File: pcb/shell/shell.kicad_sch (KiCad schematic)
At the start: 220 parts, among them J1 Conn_01x11, J2 Conn_01x11

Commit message: hid reference designators, simplified footprint silkscreens, added license, added rocks and stones
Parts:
- D1, D10, D11, D12, D13, D14, D15, D16, D17, D18, D19, D2, D20, D21, D22, D23, D24, D25, D26, D27, D28, D29, D3, D30, D31, D32, D33, D34, D35, D36, D37, D38, D39, D4, D40, D41, D42, D43, D44, D45, D46, D47, D48, D49, D5, D50, D51, D52, D53, D54, D55, D56, D57, D58, D59, D6, D60, D61, D7, D8, D9: footprint Diode_SMD:D_SOD-123 -> barnacle:D_SOD-123-minimal
- MX1, MX10, MX11, MX12, MX14, MX15, MX16, MX17, MX18, MX19, MX2, MX20, MX21, MX22, MX23, MX26, MX27, MX28, MX29, MX3, MX30, MX31, MX32, MX33, MX34, MX35, MX38, MX39, MX4, MX40, MX41, MX42, MX43, MX44, MX45, MX46, MX47, MX49, MX5, MX52, MX54, MX55, MX56, MX57, MX6, MX7, MX8, MX9: footprint PCM_marbastlib-mx:SW_MX_HS_CPG151101S11_1u -> PCM_marbastlib-mx:SW_MX_HS_S_CPG151101S11_1u
- MX13, MX24, MX61: footprint PCM_marbastlib-mx:SW_MX_HS_CPG151101S11_1.5u -> PCM_marbastlib-mx:SW_MX_HS_S_CPG151101S11_1u
- MX25, MX36, MX37: footprint PCM_marbastlib-mx:SW_MX_HS_CPG151101S11_1.75u -> PCM_marbastlib-mx:SW_MX_HS_S_CPG151101S11_1u
- MX48, MX50, MX51, MX53, MX58, MX59, MX60: footprint PCM_marbastlib-mx:SW_MX_HS_CPG151101S11_1.25u -> PCM_marbastlib-mx:SW_MX_HS_S_CPG151101S11_1u
- UG1, UG10, UG11, UG12, UG13, UG14, UG15, UG16, UG17, UG18, UG19, UG2, UG20, UG21, UG22, UG23, UG24, UG25, UG26, UG27, UG28, UG3, UG4, UG5, UG6, UG7, UG8, UG9: footprint LED_SMD:LED_SK6812_PLCC4_5.0x5.0mm_P3.2mm -> barnacle:LED_SK6812_PLCC4_5.0x5.0mm_P3.2mm-minimal

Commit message: changed sk6812 footprints to be also compatible with sk6812 mini (v1.2)
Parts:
- UG1, UG10, UG11, UG12, UG13, UG14, UG15, UG16, UG17, UG18, UG19, UG2, UG20, UG21, UG22, UG23, UG24, UG25, UG26, UG27, UG28, UG3, UG4, UG5, UG6, UG7, UG8, UG9: footprint barnacle:LED_SK6812_PLCC4_5.0x5.0mm_P3.2mm-minimal -> barnacle:LED_SK6812-combi
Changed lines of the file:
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@@
 			)
 		)
-		(property "Footprint" "barnacle:LED_SK6812_PLCC4_5.0x5.0mm_P3.2mm-minimal"
+		(property "Footprint" "barnacle:LED_SK6812-combi"
 			(at 180.34 195.58 0)
 			(effects
@@
 			)
 		)
-		(property "Footprint" "barnacle:LED_SK6812_PLCC4_5.0x5.0mm_P3.2mm-minimal"
+		(property "Footprint" "barnacle:LED_SK6812-combi"
 			(at 88.9 195.58 0)
 			(effects
@@
 			)
 		)
-		(property "Footprint" "barnacle:LED_SK6812_PLCC4_5.0x5.0mm_P3.2mm-minimal"
+		(property "Footprint" "barnacle:LED_SK6812-combi"
 			(at 134.62 195.58 0)
 			(effects
@@
 			)
 		)
-		(property "Footprint" "barnacle:LED_SK6812_PLCC4_5.0x5.0mm_P3.2mm-minimal"
+		(property "Footprint" "barnacle:LED_SK6812-combi"
 			(at 149.86 195.58 0)
 			(effects
@@
 			)
 		)
-		(property "Footprint" "barnacle:LED_SK6812_PLCC4_5.0x5.0mm_P3.2mm-minimal"
+		(property "Footprint" "barnacle:LED_SK6812-combi"
 			(at 153.67 218.44 0)
 			(effects
@@
 			)
 		)
-		(property "Footprint" "barnacle:LED_SK6812_PLCC4_5.0x5.0mm_P3.2mm-minimal"
+		(property "Footprint" "barnacle:LED_SK6812-combi"
 			(at 226.06 195.58 0)
 			(effects
@@
 			)
 		)
-		(property "Footprint" "barnacle:LED_SK6812_PLCC4_5.0x5.0mm_P3.2mm-minimal"
+		(property "Footprint" "barnacle:LED_SK6812-combi"
 			(at 210.82 195.58 0)
 			(effects
@@
 			)
 		)
-		(property "Footprint" "barnacle:LED_SK6812_PLCC4_5.0x5.0mm_P3.2mm-minimal"
+		(property "Footprint" "barnacle:LED_SK6812-combi"
 			(at 58.42 195.58 0)
 			(effects
@@
 			)
 		)
-		(property "Footprint" "barnacle:LED_SK6812_PLCC4_5.0x5.0mm_P3.2mm-minimal"
+		(property "Footprint" "barnacle:LED_SK6812-combi"
 			(at 88.9 218.44 0)
 			(effects
@@
 			)
 		)
-		(property "Footprint" "barnacle:LED_SK6812_PLCC4_5.0x5.0mm_P3.2mm-minimal"
+		(property "Footprint" "barnacle:LED_SK6812-combi"
 			(at 58.42 218.44 0)
 			(effects
@@
 			)
 		)
-		(property "Footprint" "barnacle:LED_SK6812_PLCC4_5.0x5.0mm_P3.2mm-minimal"
+		(property "Footprint" "barnacle:LED_SK6812-combi"
 			(at 153.67 172.72 0)
 			(effects
@@
 			)
 		)
-		(property "Footprint" "barnacle:LED_SK6812_PLCC4_5.0x5.0mm_P3.2mm-minimal"
+		(property "Footprint" "barnacle:LED_SK6812-combi"
 			(at 73.66 195.58 0)
 			(effects
@@
 			)
 		)
-		(property "Footprint" "barnacle:LED_SK6812_PLCC4_5.0x5.0mm_P3.2mm-minimal"
+		(property "Footprint" "barnacle:LED_SK6812-combi"
 			(at 123.19 218.44 0)
 			(effects
@@
 			)
 		)
-		(property "Footprint" "barnacle:LED_SK6812_PLCC4_5.0x5.0mm_P3.2mm-minimal"
+		(property "Footprint" "barnacle:LED_SK6812-combi"
 			(at 168.91 172.72 0)
 			(effects
@@
 			)
 		)
-		(property "Footprint" "barnacle:LED_SK6812_PLCC4_5.0x5.0mm_P3.2mm-minimal"
+		(property "Footprint" "barnacle:LED_SK6812-combi"
 			(at 88.9 172.72 0)
 			(effects
@@
 			)
 		)
-		(property "Footprint" "barnacle:LED_SK6812_PLCC4_5.0x5.0mm_P3.2mm-minimal"
+		(property "Footprint" "barnacle:LED_SK6812-combi"
 			(at 195.58 195.58 0)
 			(effects
@@
 			)
 		)
-		(property "Footprint" "barnacle:LED_SK6812_PLCC4_5.0x5.0mm_P3.2mm-minimal"
+		(property "Footprint" "barnacle:LED_SK6812-combi"
 			(at 104.14 195.58 0)
 			(effects
@@
 			)
 		)
-		(property "Footprint" "barnacle:LED_SK6812_PLCC4_5.0x5.0mm_P3.2mm-minimal"
+		(property "Footprint" "barnacle:LED_SK6812-combi"
 			(at 104.14 172.72 0)
 			(effects
@@
 			)
 		)
-		(property "Footprint" "barnacle:LED_SK6812_PLCC4_5.0x5.0mm_P3.2mm-minimal"
+		(property "Footprint" "barnacle:LED_SK6812-combi"
 			(at 119.38 195.58 0)
 			(effects
@@
 			)
 		)
-		(property "Footprint" "barnacle:LED_SK6812_PLCC4_5.0x5.0mm_P3.2mm-minimal"
+		(property "Footprint" "barnacle:LED_SK6812-combi"
 			(at 168.91 218.44 0)
 			(effects
@@
 			)
 		)
-		(property "Footprint" "barnacle:LED_SK6812_PLCC4_5.0x5.0mm_P3.2mm-minimal"
+		(property "Footprint" "barnacle:LED_SK6812-combi"
 			(at 73.66 172.72 0)
 			(effects
@@
 			)
 		)
-		(property "Footprint" "barnacle:LED_SK6812_PLCC4_5.0x5.0mm_P3.2mm-minimal"
+		(property "Footprint" "barnacle:LED_SK6812-combi"
 			(at 73.66 218.44 0)
 			(effects
@@
 			)
 		)
-		(property "Footprint" "barnacle:LED_SK6812_PLCC4_5.0x5.0mm_P3.2mm-minimal"
+		(property "Footprint" "barnacle:LED_SK6812-combi"
 			(at 58.42 172.72 0)
 			(effects
@@
 			)
 		)
-		(property "Footprint" "barnacle:LED_SK6812_PLCC4_5.0x5.0mm_P3.2mm-minimal"
+		(property "Footprint" "barnacle:LED_SK6812-combi"
 			(at 138.43 172.72 0)
 			(effects
@@
 			)
 		)
-		(property "Footprint" "barnacle:LED_SK6812_PLCC4_5.0x5.0mm_P3.2mm-minimal"
+		(property "Footprint" "barnacle:LED_SK6812-combi"
 			(at 119.38 172.72 0)
 			(effects
@@
 			)
 		)
-		(property "Footprint" "barnacle:LED_SK6812_PLCC4_5.0x5.0mm_P3.2mm-minimal"
+		(property "Footprint" "barnacle:LED_SK6812-combi"
 			(at 165.1 195.58 0)
 			(effects
@@
 			)
 		)
-		(property "Footprint" "barnacle:LED_SK6812_PLCC4_5.0x5.0mm_P3.2mm-minimal"
+		(property "Footprint" "barnacle:LED_SK6812-combi"
 			(at 107.95 218.44 0)
 			(effects
@@
 			)
 		)
-		(property "Footprint" "barnacle:LED_SK6812_PLCC4_5.0x5.0mm_P3.2mm-minimal"
+		(property "Footprint" "barnacle:LED_SK6812-combi"
 			(at 138.43 218.44 0)
 			(effects

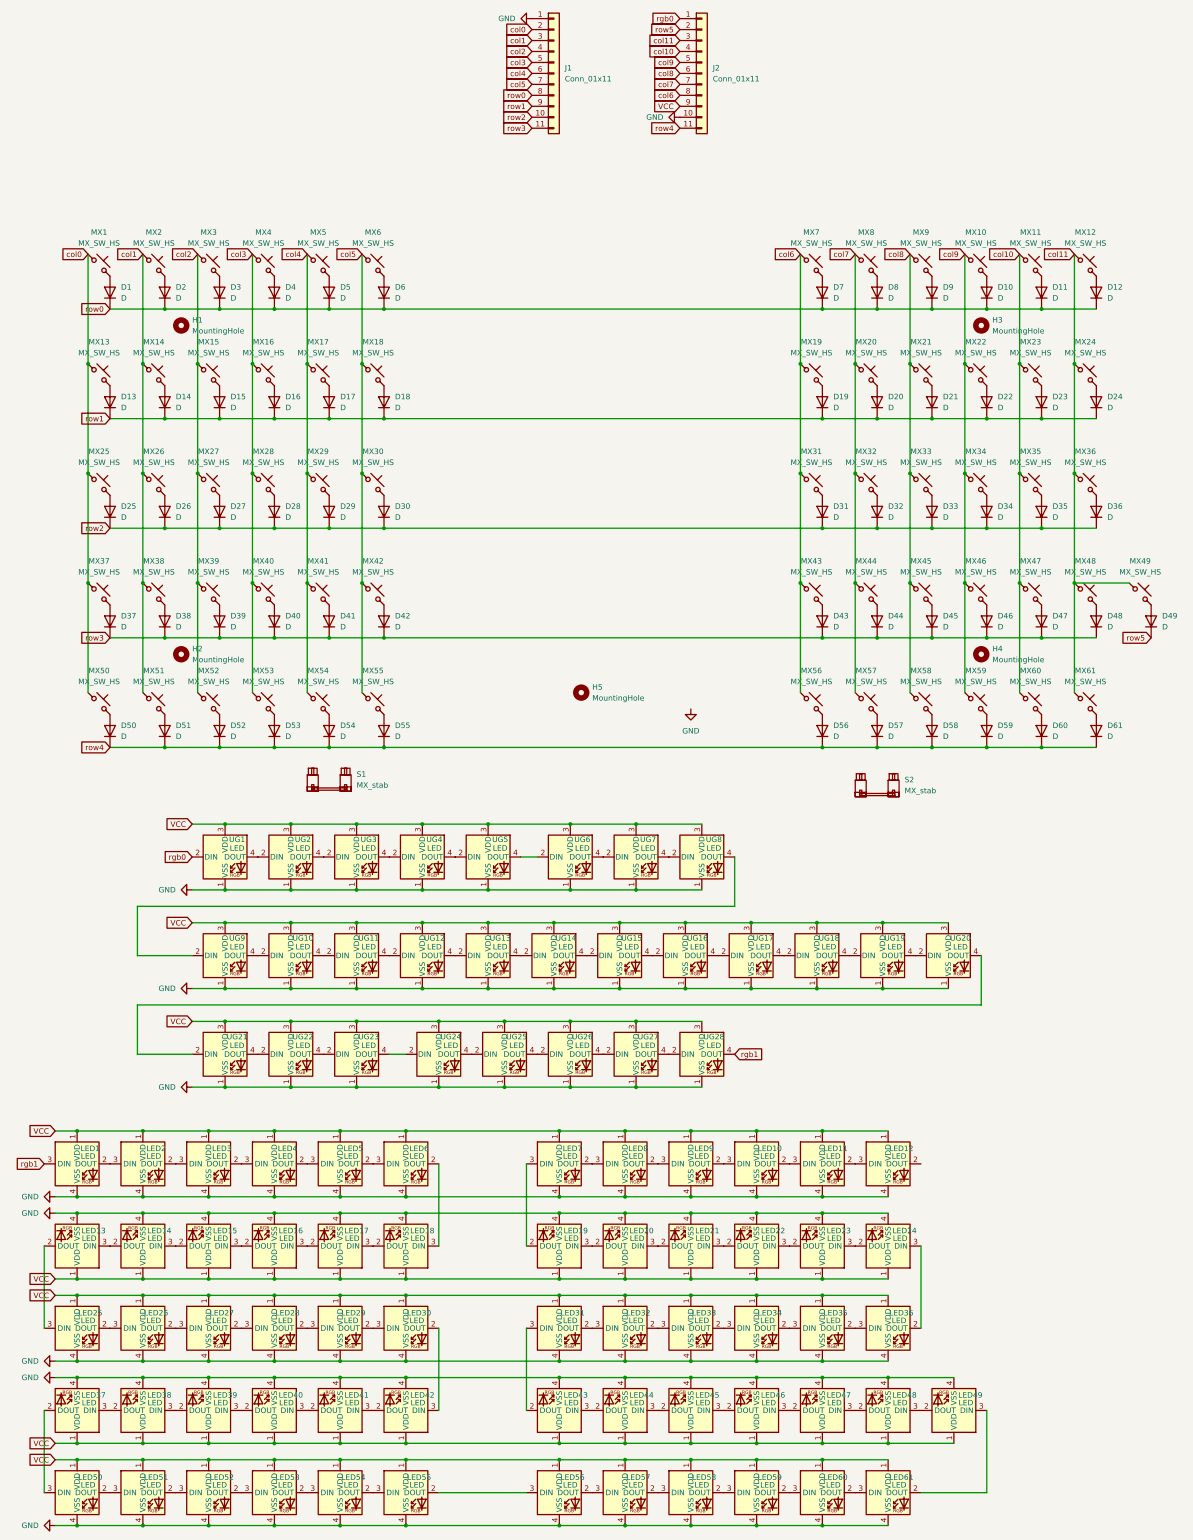
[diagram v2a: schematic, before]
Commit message: updated pcb to only use sk6812 mini-e
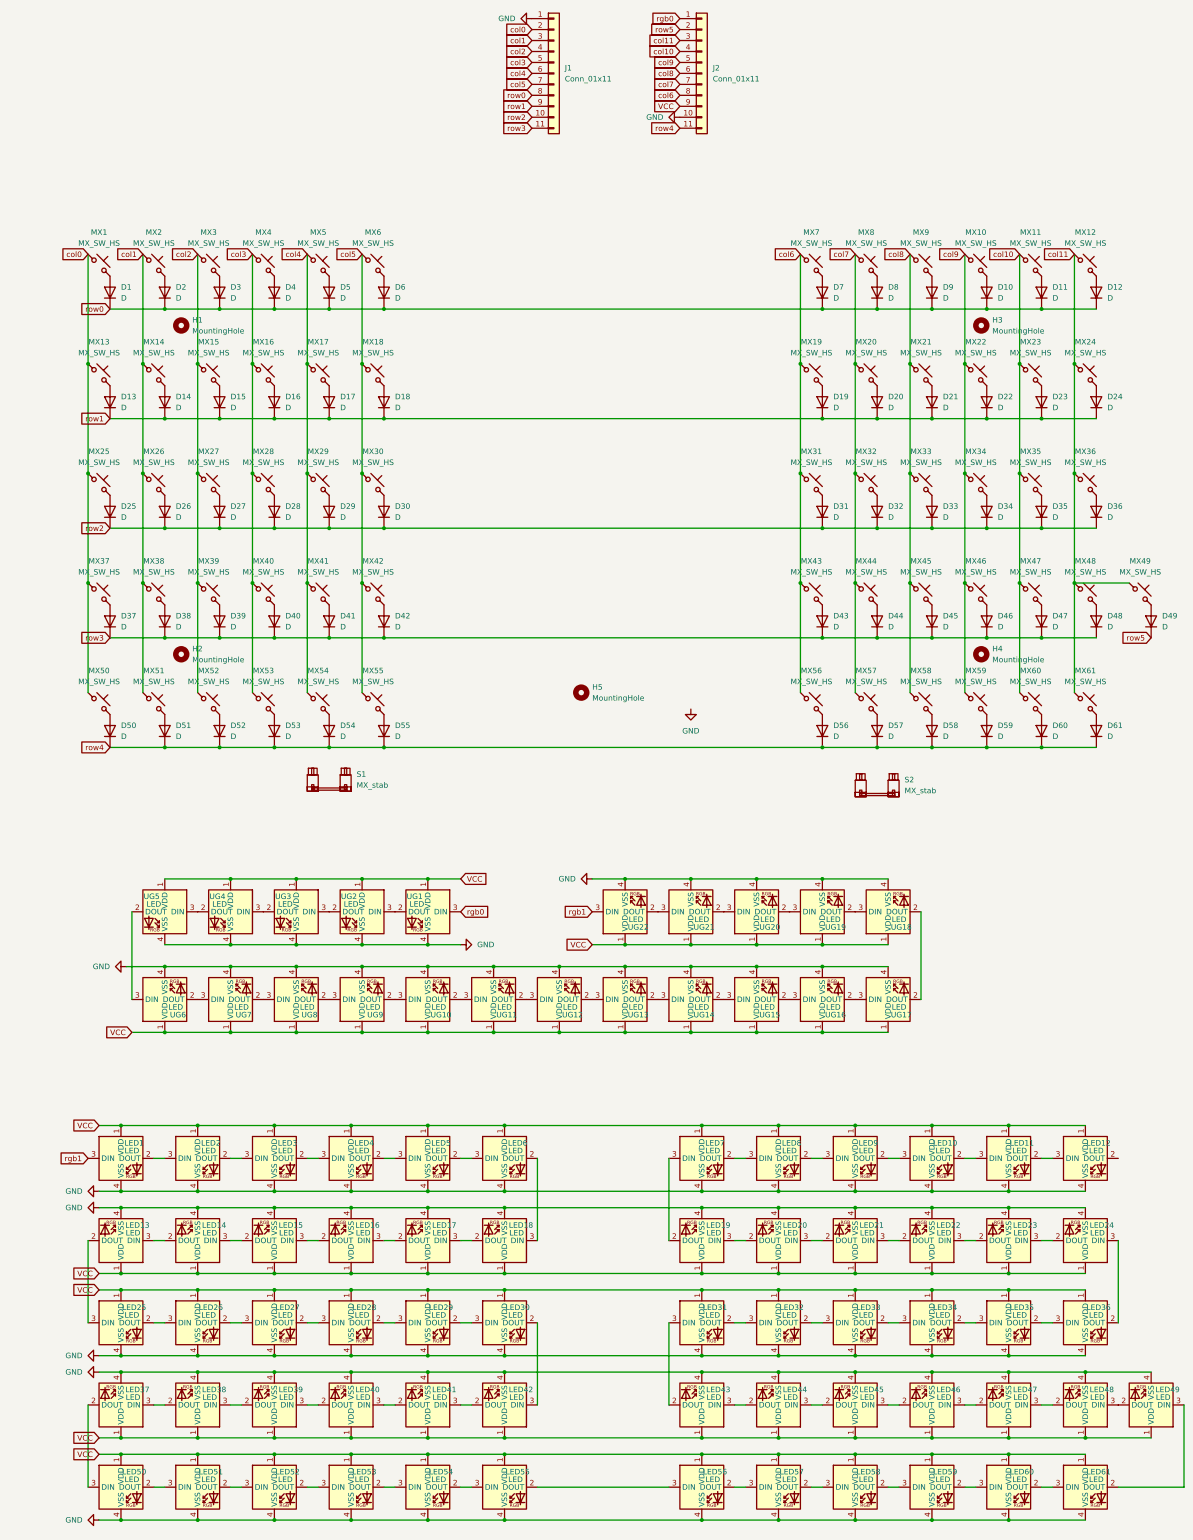
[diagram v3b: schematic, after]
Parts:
- removed UG1, UG10, UG11, UG12, UG13, UG14, UG15, UG16, UG17, UG18, UG19, UG2, UG20, UG21, UG22, UG23, UG24, UG25, UG26, UG27, UG28, UG3, UG4, UG5, UG6, UG7, UG8, UG9: LED, barnacle:LED_SK6812-combi, symbol LED:SK6812
- added UG1, UG10, UG11, UG12, UG13, UG14, UG15, UG16, UG17, UG18, UG19, UG2, UG20, UG21, UG22, UG3, UG4, UG5, UG6, UG7, UG8, UG9: LED, barnacle:sk6812 mini-e towards-facing, symbol PCM_marbastlib-mx:MX_SK6812MINI-E
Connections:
- net GND: now also UG1.4 (VSS), UG10.4 (VSS), UG11.4 (VSS), UG12.4 (VSS), UG13.4 (VSS), UG14.4 (VSS), UG15.4 (VSS), UG16.4 (VSS), UG17.4 (VSS), UG18.4 (VSS), UG19.4 (VSS), UG2.4 (VSS), UG20.4 (VSS), UG21.4 (VSS), UG22.4 (VSS), UG3.4 (VSS), UG4.4 (VSS), UG5.4 (VSS), UG6.4 (VSS), UG7.4 (VSS), UG8.4 (VSS), UG9.4 (VSS)
- net VCC: now also UG1.1 (VDD), UG10.1 (VDD), UG11.1 (VDD), UG12.1 (VDD), UG13.1 (VDD), UG14.1 (VDD), UG15.1 (VDD), UG16.1 (VDD), UG17.1 (VDD), UG18.1 (VDD), UG19.1 (VDD), UG2.1 (VDD), UG20.1 (VDD), UG21.1 (VDD), UG22.1 (VDD), UG3.1 (VDD), UG4.1 (VDD), UG5.1 (VDD), UG6.1 (VDD), UG7.1 (VDD), UG8.1 (VDD), UG9.1 (VDD)
- net rgb0: now also UG1.3 (DIN)
- net rgb1: now also UG22.3 (DIN)
- new net: UG14.2 (DOUT), UG15.3 (DIN)
- new net: UG13.2 (DOUT), UG14.3 (DIN)
- new net: UG20.3 (DIN), UG21.2 (DOUT)
- new net: UG21.3 (DIN), UG22.2 (DOUT)
- new net: UG7.2 (DOUT), UG8.3 (DIN)
- new net: UG6.2 (DOUT), UG7.3 (DIN)
- new net: UG17.2 (DOUT), UG18.2 (DOUT)
- new net: UG16.2 (DOUT), UG17.3 (DIN)
- new net: UG4.2 (DOUT), UG5.3 (DIN)
- new net: UG3.2 (DOUT), UG4.3 (DIN)
- new net: UG2.2 (DOUT), UG3.3 (DIN)
- new net: UG1.2 (DOUT), UG2.3 (DIN)
- new net: UG19.3 (DIN), UG20.2 (DOUT)
- new net: UG12.2 (DOUT), UG13.3 (DIN)
- new net: UG11.2 (DOUT), UG12.3 (DIN)
- new net: UG5.2 (DOUT), UG6.3 (DIN)
- new net: UG10.2 (DOUT), UG11.3 (DIN)
- new net: UG15.2 (DOUT), UG16.3 (DIN)
- new net: UG8.2 (DOUT), UG9.3 (DIN)
- new net: UG18.3 (DIN), UG19.2 (DOUT)
- new net: UG10.3 (DIN), UG9.2 (DOUT)
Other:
- moved on the sheet: LED1, LED10, LED11, LED12, LED13, LED14, LED15, LED16, LED17, LED18, LED19, LED2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

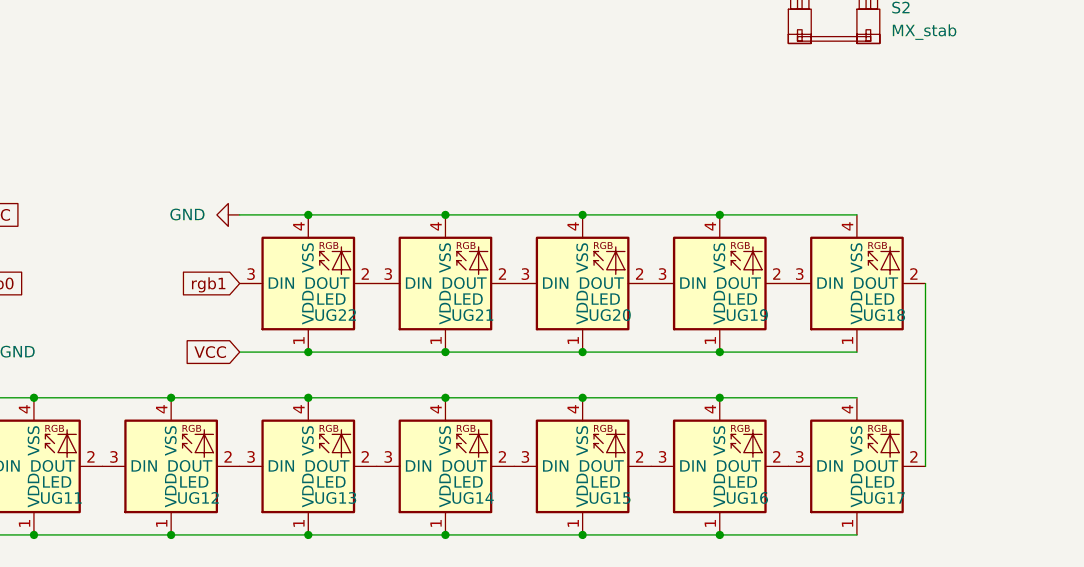
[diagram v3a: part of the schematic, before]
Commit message: fixed rotation of top row underglow leds
sigh…
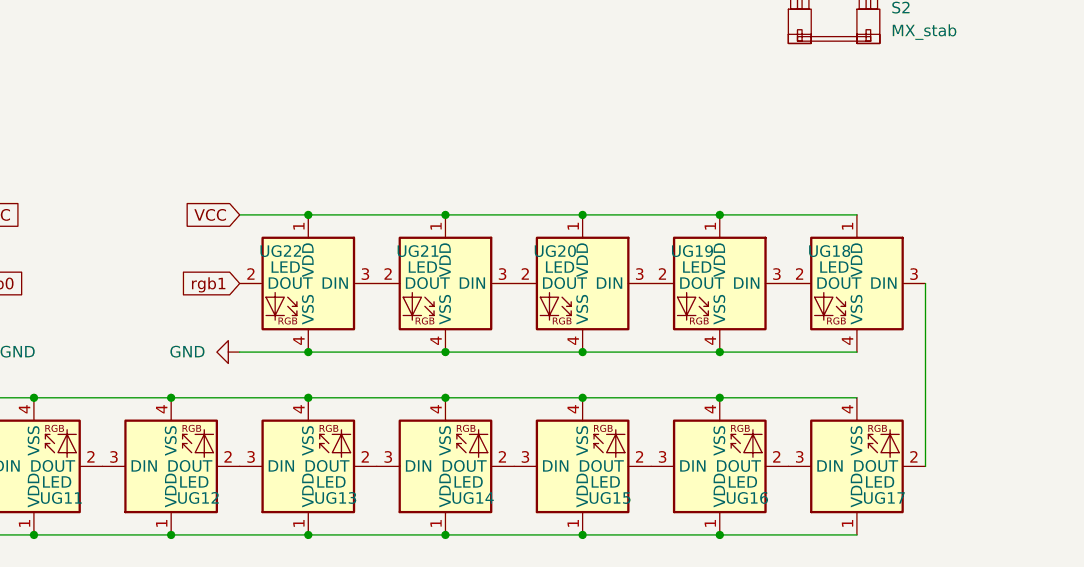
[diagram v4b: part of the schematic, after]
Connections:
- net rgb1: now also UG22.2 (DOUT); no longer UG22.3 (DIN)
- net at UG21.2 (DOUT): now also UG22.3 (DIN); no longer UG20.3 (DIN)
- net at UG21.3 (DIN): now also UG20.2 (DOUT); no longer UG22.2 (DOUT)
- net at UG17.2 (DOUT): now also UG18.3 (DIN); no longer UG18.2 (DOUT)
- net at UG19.3 (DIN): now also UG18.2 (DOUT); no longer UG20.2 (DOUT)
- net at UG19.2 (DOUT): now also UG20.3 (DIN); no longer UG18.3 (DIN)
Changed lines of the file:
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@@
 	(global_label "VCC"
 		(shape input)
-		(at 142.24 185.42 180)
+		(at 142.24 170.18 180)
 		(fields_autoplaced yes)
 		(effects
@@
 		)
 		(property "Intersheetrefs" "${INTERSHEET_REFS}"
-			(at 135.6262 185.42 0)
+			(at 135.6262 170.18 0)
 			(effects
 				(font
@@
 		(lib_id "PCM_marbastlib-mx:MX_SK6812MINI-E")
 		(at 165.1 177.8 0)
-		(mirror x)
+		(mirror y)
 		(unit 1)
 		(exclude_from_sim no)
@@
 		(dnp no)
 		(property "Reference" "UG21"
-			(at 168.148 181.356 0)
+			(at 162.052 174.244 0)
 			(effects
 				(font
@@
 		)
 		(property "Value" "LED"
-			(at 167.64 179.578 0)
+			(at 162.56 176.022 0)
 			(effects
 				(font
@@
 		(lib_id "PCM_marbastlib-mx:MX_SK6812MINI-E")
 		(at 180.34 177.8 0)
-		(mirror x)
+		(mirror y)
 		(unit 1)
 		(exclude_from_sim no)
@@
 		(dnp no)
 		(property "Reference" "UG20"
-			(at 183.388 181.356 0)
+			(at 177.292 174.244 0)
 			(effects
 				(font
@@
 		)
 		(property "Value" "LED"
-			(at 182.88 179.578 0)
+			(at 177.8 176.022 0)
 			(effects
 				(font
@@
 	(symbol
 		(lib_id "power:GND")
-		(at 142.24 170.18 270)
+		(at 142.24 185.42 270)
 		(unit 1)
 		(exclude_from_sim no)
@@
 		(fields_autoplaced yes)
 		(property "Reference" "#PWR010"
-			(at 135.89 170.18 0)
+			(at 135.89 185.42 0)
 			(effects
 				(font
@@
 		)
 		(property "Value" "GND"
-			(at 138.43 170.1799 90)
+			(at 138.43 185.4199 90)
 			(effects
 				(font
@@
 		)
 		(property "Footprint" ""
-			(at 142.24 170.18 0)
+			(at 142.24 185.42 0)
 			(effects
 				(font
@@
 		)
 		(property "Datasheet" ""
-			(at 142.24 170.18 0)
+			(at 142.24 185.42 0)
 			(effects
 				(font
@@
 		)
 		(property "Description" "Power symbol creates a global label with name \"GND\" , ground"
-			(at 142.24 170.18 0)
+			(at 142.24 185.42 0)
 			(effects
 				(font
@@
 		(lib_id "PCM_marbastlib-mx:MX_SK6812MINI-E")
 		(at 195.58 177.8 0)
-		(mirror x)
+		(mirror y)
 		(unit 1)
 		(exclude_from_sim no)
@@
 		(dnp no)
 		(property "Reference" "UG19"
-			(at 198.628 181.356 0)
+			(at 192.532 174.244 0)
 			(effects
 				(font
@@
 		)
 		(property "Value" "LED"
-			(at 198.12 179.578 0)
+			(at 193.04 176.022 0)
 			(effects
 				(font
@@
 		(lib_id "PCM_marbastlib-mx:MX_SK6812MINI-E")
 		(at 149.86 177.8 0)
-		(mirror x)
+		(mirror y)
 		(unit 1)
 		(exclude_from_sim no)
@@
 		(dnp no)
 		(property "Reference" "UG22"
-			(at 152.908 181.356 0)
+			(at 146.812 174.244 0)
 			(effects
 				(font
@@
 		)
 		(property "Value" "LED"
-			(at 152.4 179.578 0)
+			(at 147.32 176.022 0)
 			(effects
 				(font
@@
 		(lib_id "PCM_marbastlib-mx:MX_SK6812MINI-E")
 		(at 210.82 177.8 0)
-		(mirror x)
+		(mirror y)
 		(unit 1)
 		(exclude_from_sim no)
@@
 		(dnp no)
 		(property "Reference" "UG18"
-			(at 213.868 181.356 0)
+			(at 207.772 174.244 0)
 			(effects
 				(font
@@
 		)
 		(property "Value" "LED"
-			(at 213.36 179.578 0)
+			(at 208.28 176.022 0)
 			(effects
 				(font
